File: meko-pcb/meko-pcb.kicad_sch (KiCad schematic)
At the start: 208 parts, among them IC2 TPS7A2033PDBVR, IC4 TAD5212IRGER, IC5 AS5600-ASOM, J1 USB_C_Receptacle_USB2.0_16P, J2 Conn_ARM_JTAG_SWD_10, J3 GDEY0154D67, J5 503398-1892, Q1 SS8050, Q2 Si1308EDL, SW1 SW_Push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

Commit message: made final changes
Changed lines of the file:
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@@
 	(wire
 		(pts
-			(xy 177.8 275.59) (xy 234.95 275.59)
-		)
-		(stroke
-			(width 0)
-			(type default)
-		)
-	)
-	(wire
-		(pts
 			(xy 157.48 275.59) (xy 166.37 275.59)
 		)
@@
 	(wire
 		(pts
+			(xy 177.8 275.59) (xy 234.95 275.59)
+		)
+		(stroke
+			(width 0)
+			(type default)
+		)
+	)
+	(wire
+		(pts
 			(xy 370.84 354.33) (xy 386.08 354.33)
 		)
@@
 		)
 		(property "Value" "+3V3AVDD"
-			(at 295.148 134.62 0)
+			(at 292.608 136.398 0)
 			(effects
 				(font

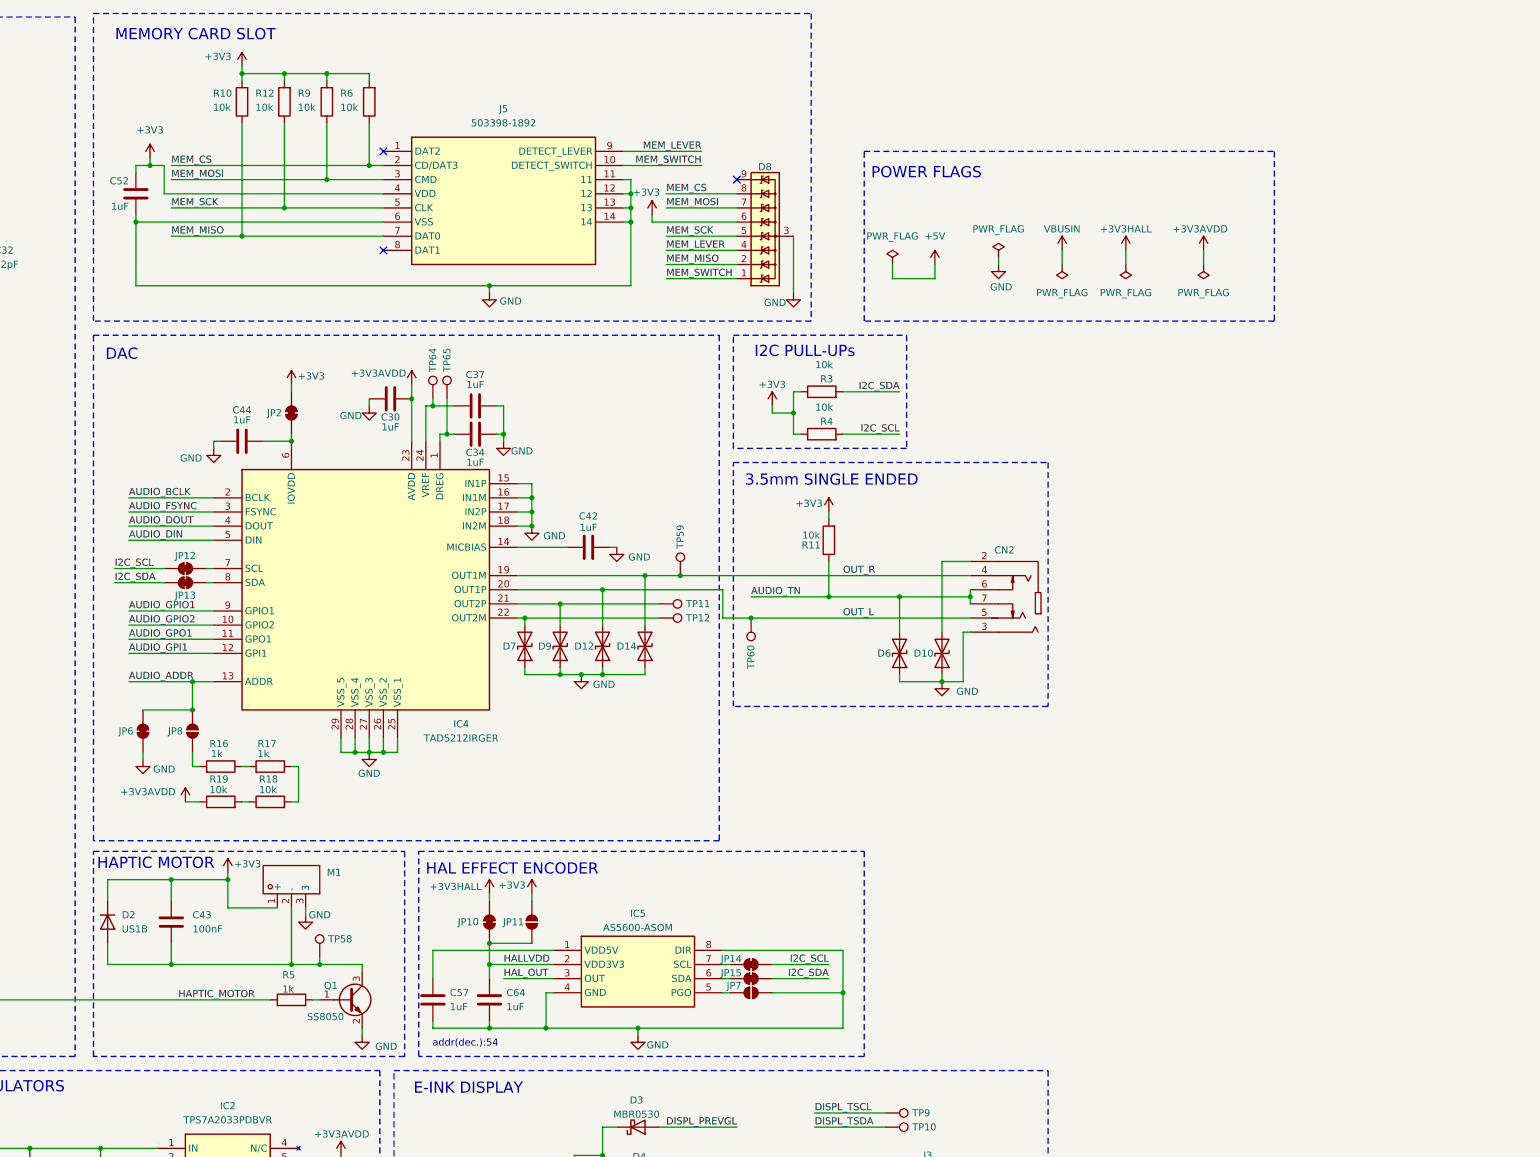
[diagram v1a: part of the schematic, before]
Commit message: fixed mistake in asom
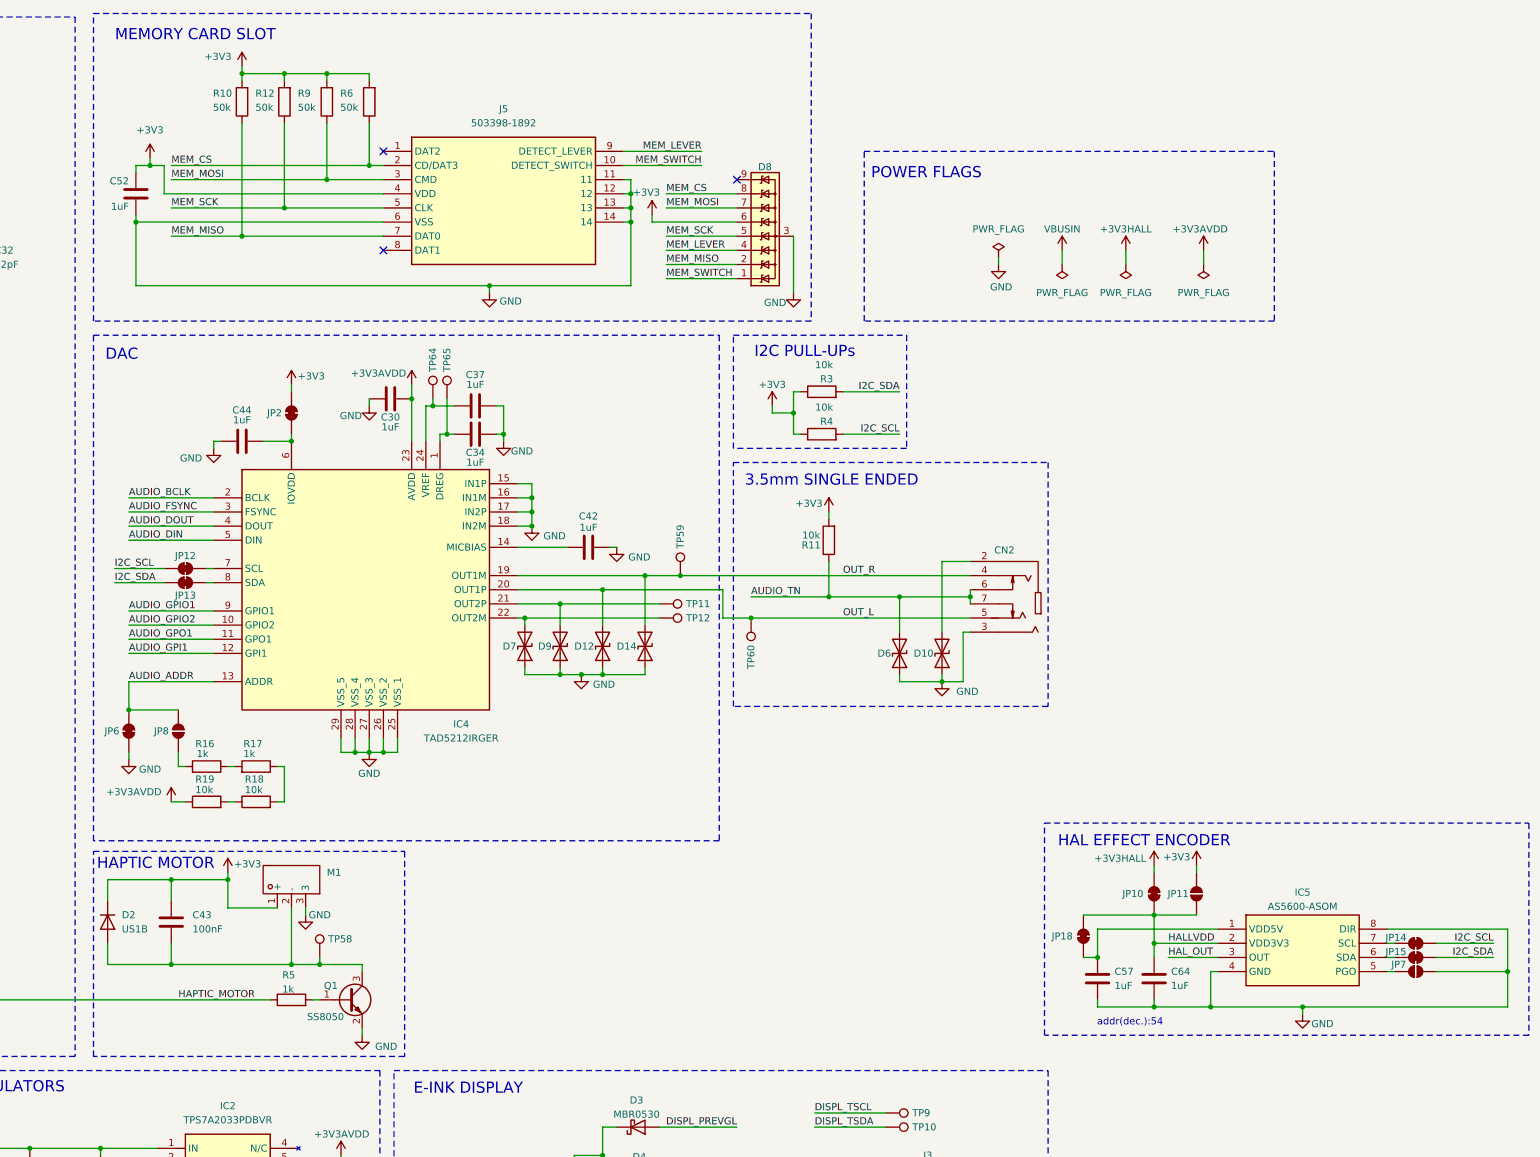
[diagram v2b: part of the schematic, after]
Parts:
- added JP18: SolderJumper_2_Bridged, Jumper:SolderJumper-2_P1.3mm_Bridged_RoundedPad1.0x1.5mm, symbol Jumper:SolderJumper_2_Bridged
- R10, R12, R6, R9: value 10k -> 50k; MPN CRCW040210K0FKED -> (none)
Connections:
- net HALLVDD: now also JP18.2 (B)
- net at C57.1, IC5.1 (VDD5V): now also JP18.1 (A)
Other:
- moved on the sheet: C57, C64, IC5, JP10, JP11, JP14, JP15, JP6, JP7, JP8, R16, R17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

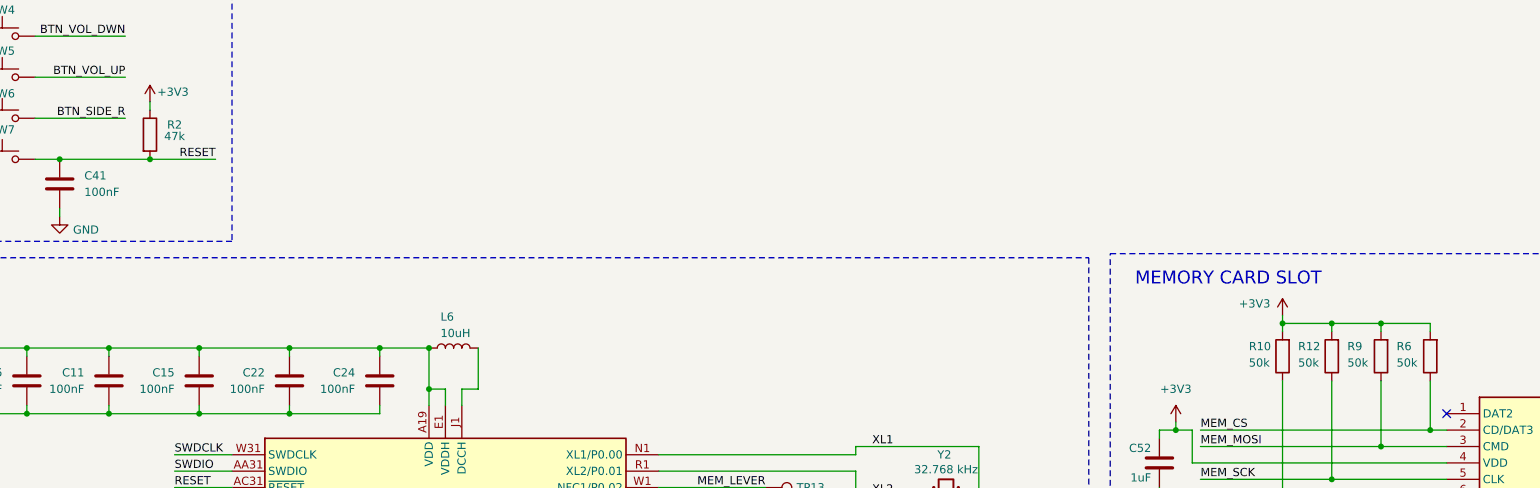
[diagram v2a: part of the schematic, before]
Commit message: assigned all the mpns and lcsc numbers
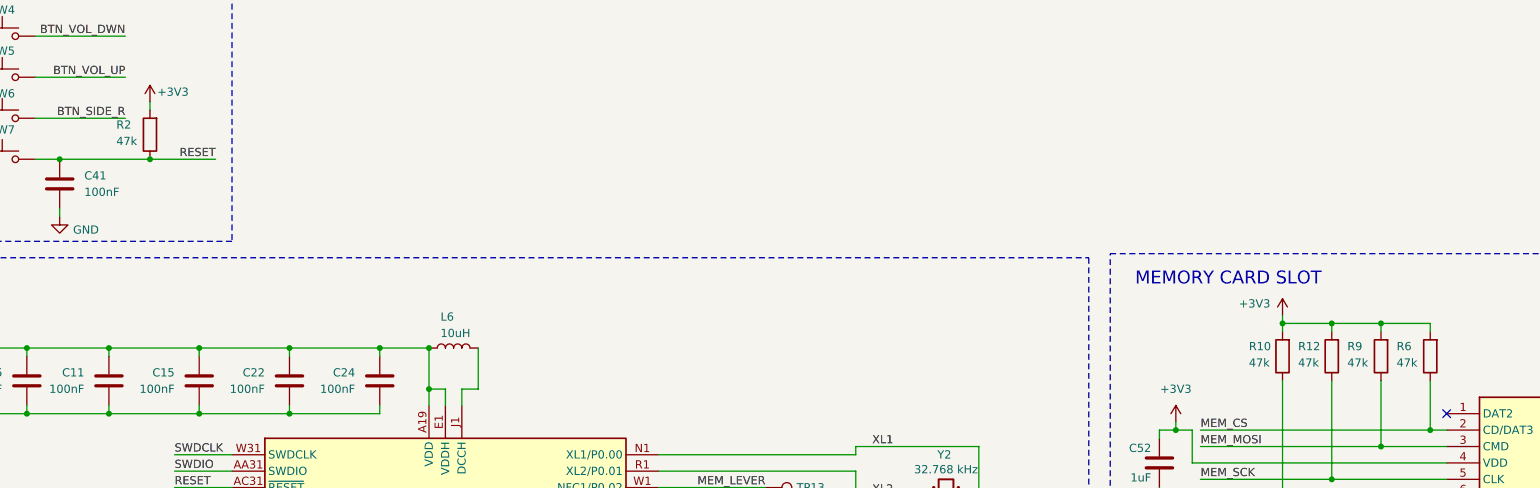
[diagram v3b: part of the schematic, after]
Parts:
- AE1: LCSC (none) -> C293767
- C1, C10, C11, C14, C15, C19, C2, C22, C24, C4, C41, C43, C6: LCSC (none) -> C14663; MPN CL05B104KO5NNNC -> CC0603KRX7R9BB104
- C12, C20: LCSC (none) -> C15849; MPN CL05B104KO5NNNC -> CL10A105KB8NNNC
- C13: MPN CL05B104KO5NNNC -> (none); now left out of the parts list
- C16, C21, C23, C25, C26, C27: LCSC (none) -> C19702; MPN CL05A106MQ5NUNC -> CL10A106KP8NNNC
- C17: LCSC (none) -> C5137562; MPN CL05B104KO5NNNC -> FCC0603B222K500CT
- C18: LCSC (none) -> C519367; MPN CL05B104KO5NNNC -> CC0603BRNPO9BNR70
- C28, C30, C34, C35, C37, C39, C42, C44, C45, C49, C50, C51, C52, C53, C54, C55, C57, C61, C62, C63, C64: LCSC (none) -> C15849; MPN CL05A105KO5NNNC -> CL10A105KB8NNNC
- C3: LCSC (none) -> C15849; MPN CL05A106MQ5NUNC -> CL10A105KB8NNNC
- C31, C32, C7, C8: LCSC (none) -> C38523; MPN (none) -> CL10C120JB8NNNC
- C5, C9: LCSC (none) -> C1705; MPN CL05B104KO5NNNC -> CL10A475KP8NNNC
- CN2: LCSC (none) -> C668606; MPN (none) -> PJ-342; Manufacturer Part PJ-342 -> (none)
- D1: LCSC (none) -> C12333; MPN (none) -> PRTR5V0U2X,215
- D10, D12, D14, D6, D7, D9: LCSC (none) -> C29779756
- D11: LCSC (none) -> C965800
- D15: LCSC (none) -> C965808
- D16: LCSC (none) -> C7496823
- D2: LCSC (none) -> C18199126
- D3, D4, D5: LCSC (none) -> C82046
- D8: LCSC (none) -> C3715130
- IC2: LCSC (none) -> C2862740
- IC4: LCSC (none) -> C45068920; MPN (none) -> TAD5212IRGER; Manufacturer_Part_Number TAD5112IRGER -> (none)
- IC5: LCSC (none) -> C499458
- J1: LCSC (none) -> C2988369
- J2: now left out of the parts list
- J3: LCSC (none) -> C2856831; Manufacturer_Part_Number FH34SRJ-24S-0.5SH(99) -> (none)
- J5: LCSC (none) -> C428492
- L1: LCSC (none) -> C113061; MPN 1239AS-H-100M=P2 -> LQG18HN2N2S00D
- L2, L3, L6: footprint Inductor_SMD:L_1008_2520Metric -> Inductor_SMD:L_0805_2012Metric; LCSC (none) -> C2831365; MPN 1239AS-H-100M=P2 -> SLM2012100MIT
- L4, L5: LCSC (none) -> C2049745
- L7: LCSC (none) -> C383408
- M1: MPN (none) -> LD-SM-430; Manufacturer Part LD-SM-430 -> (none)
- Q1: LCSC (none) -> C5179688
- Q2: LCSC (none) -> C469327
- R1: LCSC (none) -> C2930091; MPN (none) -> FRC0603F3003TS
- R10, R12, R6, R9: value 50k -> 47k; LCSC (none) -> C2907042; MPN (none) -> FRC0603F4702TS
- R11, R18, R19, R3, R4: LCSC (none) -> C25804; MPN CRCW040210K0FKED -> 0603WAF1002T5E
- R13, R14, R15: LCSC (none) -> C107696; MPN CRCW040210K0FKED -> RC0603FR-07220RL
- R16, R17, R5: LCSC (none) -> C22548; MPN RC0402FR-071KL -> RC0603FR-071KL
- R2: LCSC (none) -> C2907042; MPN RC0402FR-0747KL -> FRC0603F4702TS
- R7: LCSC (none) -> C105578; MPN RC0402FR-071ML -> RC0603FR-071ML
- R8: LCSC (none) -> C2930032; MPN RC0402FR-072R2L -> FRC0603J2R2TS
- SW1, SW7, SW9: LCSC (none) -> C720477
- SW2, SW3, SW4, SW5, SW6: LCSC (none) -> C110293
- U1: LCSC (none) -> C7501206; MPN (none) -> nPM1300-QEAA-R7
- U2: LCSC (none) -> C3015611; MPN (none) -> NRF5340-QKAA-R
- Y1: LCSC (none) -> C2149238
- Y2: LCSC (none) -> C5213671; MPN XKXGI-SUA-32.768K -> XKXGI-SUA-32.768K
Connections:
- net +3V3: now also R2.2; no longer R2.1
- net RESET: now also R2.1; no longer R2.2

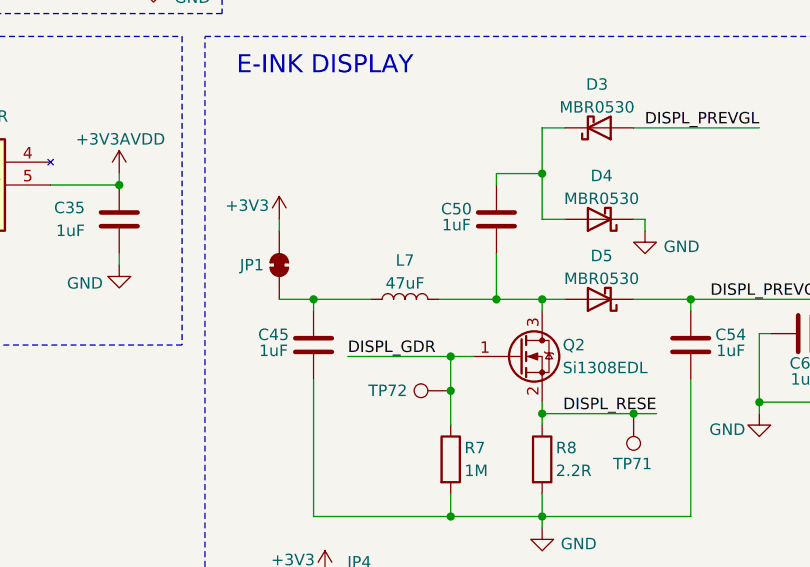
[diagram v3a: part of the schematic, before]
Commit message: optimzed bom
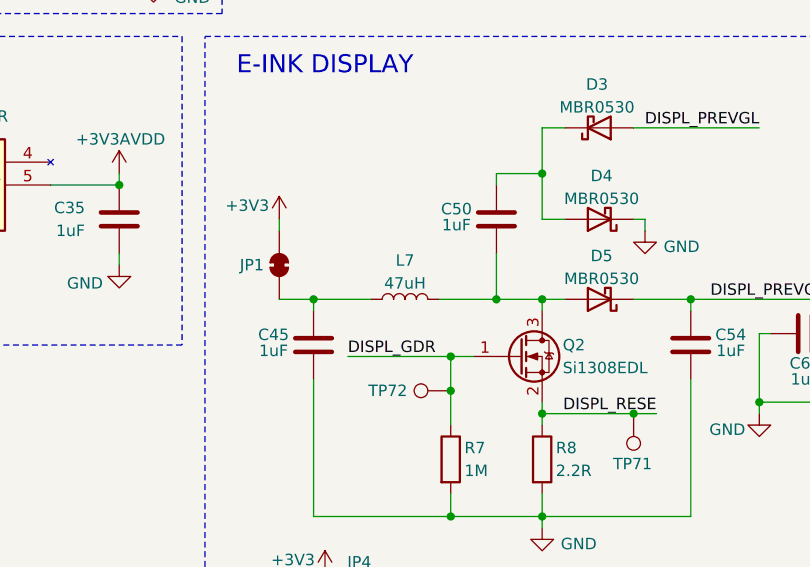
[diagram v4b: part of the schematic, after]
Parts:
- C5, C9: LCSC C1705 -> C19666
- L7: value 47uF -> 47uH
- R1: LCSC C2930091 -> C23024
- R10, R12, R2, R6, R9: LCSC C2907042 -> C25819
- R13, R14, R15: LCSC C107696 -> C22962
- R16, R17, R5: LCSC C22548 -> C21190
- R7: LCSC C105578 -> C22935
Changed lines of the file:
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@@
 			)
 		)
-		(property "LCSC" "C2907042"
+		(property "LCSC" "C25819"
 			(at 280.67 87.63 0)
 			(effects
@@
 			)
 		)
-		(property "LCSC" "C2907042"
+		(property "LCSC" "C25819"
 			(at 273.05 87.63 0)
 			(effects
@@
 			)
 		)
-		(property "LCSC" "C105578"
+		(property "LCSC" "C22935"
 			(at 327.66 308.61 0)
 			(effects
@@
 			)
 		)
-		(property "LCSC" "C2930091"
+		(property "LCSC" "C23024"
 			(at 100.33 353.06 0)
 			(effects
@@
 			)
 		)
-		(property "LCSC" "C107696"
+		(property "LCSC" "C22962"
 			(at 92.71 318.77 90)
 			(effects
@@
 			)
 		)
-		(property "LCSC" "C2907042"
+		(property "LCSC" "C25819"
 			(at 288.29 87.63 0)
 			(effects
@@
 			)
 		)
-		(property "LCSC" "C22548"
+		(property "LCSC" "C21190"
 			(at 275.59 207.01 90)
 			(effects
@@
 			)
 		)
-		(property "LCSC" "C22548"
+		(property "LCSC" "C21190"
 			(at 281.94 248.92 90)
 			(effects
@@
 			)
 		)
-		(property "LCSC" "C22548"
+		(property "LCSC" "C21190"
 			(at 266.7 207.01 90)
 			(effects
@@
 			)
 		)
-		(property "Value" "47uF"
+		(property "Value" "47uH"
 			(at 322.58 289.052 90)
 			(effects
@@
 			)
 		)
-		(property "LCSC" "C2907042"
+		(property "LCSC" "C25819"
 			(at 295.91 87.63 0)
 			(effects
@@
 			)
 		)
-		(property "LCSC" "C1705"
+		(property "LCSC" "C19666"
 			(at 67.31 240.03 0)
 			(effects
@@
 			)
 		)
-		(property "LCSC" "C1705"
+		(property "LCSC" "C19666"
 			(at 81.28 240.03 0)
 			(effects
@@
 			)
 		)
-		(property "LCSC" "C107696"
+		(property "LCSC" "C22962"
 			(at 92.71 314.96 90)
 			(effects
@@
 			)
 		)
-		(property "LCSC" "C107696"
+		(property "LCSC" "C22962"
 			(at 92.71 311.15 90)
 			(effects
@@
 			)
 		)
-		(property "LCSC" "C2907042"
+		(property "LCSC" "C25819"
 			(at 97.79 53.34 0)
 			(effects

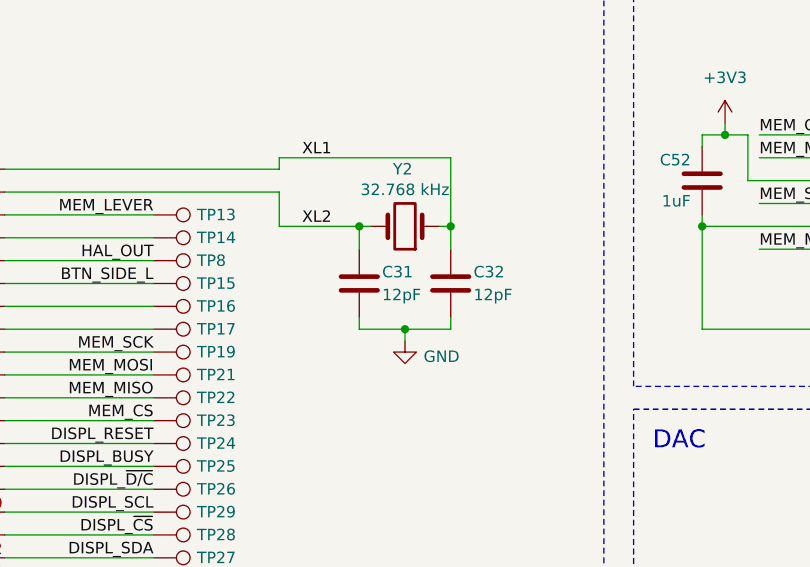
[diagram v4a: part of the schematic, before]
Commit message: made load caps dnp, cuz the nrf has internal ones
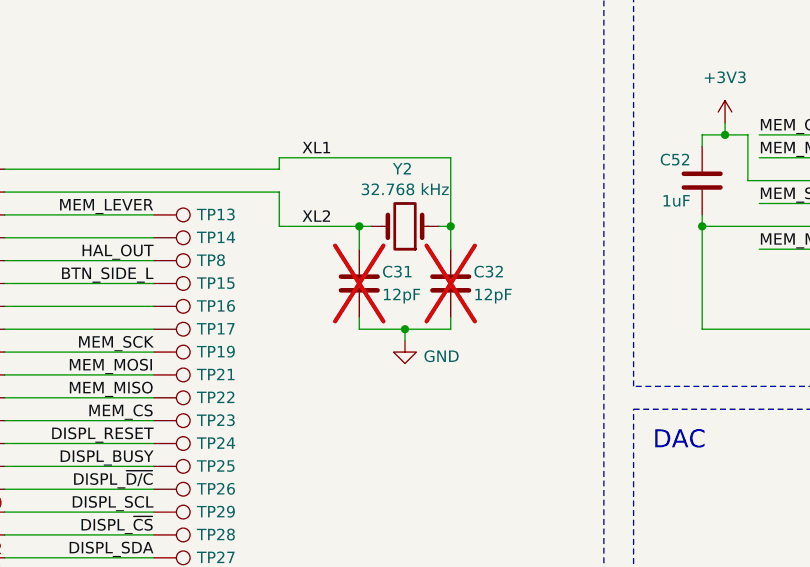
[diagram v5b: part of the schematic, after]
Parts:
- C31, C32: now not fitted; now left out of the parts list
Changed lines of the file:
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@@
 		(unit 1)
 		(exclude_from_sim no)
-		(in_bom yes)
+		(in_bom no)
 		(on_board yes)
-		(dnp no)
+		(dnp yes)
 		(property "Reference" "C32"
 			(at 228.6 114.3 0)
@@
 		(unit 1)
 		(exclude_from_sim no)
-		(in_bom yes)
+		(in_bom no)
 		(on_board yes)
-		(dnp no)
+		(dnp yes)
 		(property "Reference" "C31"
 			(at 218.44 114.3 0)
